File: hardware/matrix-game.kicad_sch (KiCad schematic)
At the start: 31 parts, among them SW1 button_center, SW2 button_left, SW3 button_down, SW4 button_right, SW5 button_up, U1 NUCLEO-F042K6, U2 MAX7219, U3 DM-OLED096-636

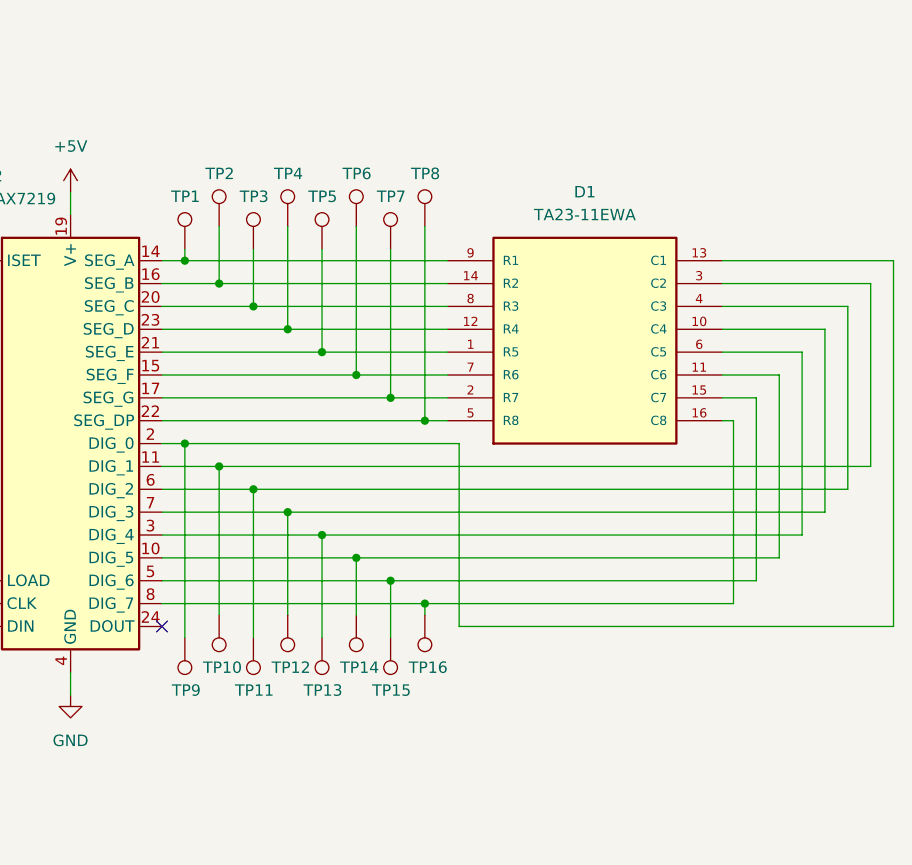
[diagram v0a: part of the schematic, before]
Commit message: [hardware] Replaced old TP pins with a 1x16, 2.54mm pin header
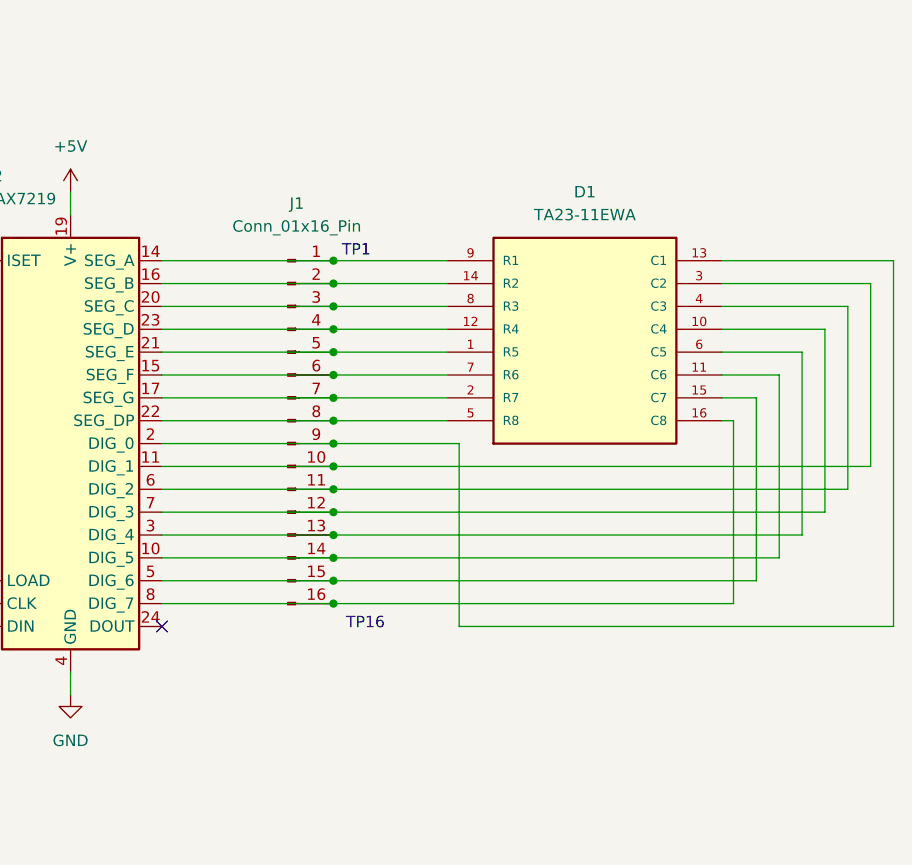
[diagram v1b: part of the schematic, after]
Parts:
- removed TP1, TP10, TP11, TP12, TP13, TP14, TP15, TP16, TP2, TP3, TP4, TP5, TP6, TP7, TP8, TP9: TestPoint, Connector_PinHeader_2.54mm:PinHeader_1x01_P2.54mm_Vertical, symbol Connector:TestPoint
- added J1: Conn_01x16_Pin, Connector_PinHeader_2.54mm:PinHeader_1x16_P2.54mm_Vertical, symbol Connector:Conn_01x16_Pin
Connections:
- net at D1.14 (R2), U2.16 (SEG_B): now also J1.2 (Pin_2)
- net at D1.9 (R1), U2.14 (SEG_A): now also J1.1 (Pin_1)
- net at D1.7 (R6), U2.15 (SEG_F): now also J1.6 (Pin_6)
- net at D1.4 (C3), U2.6 (DIG_2): now also J1.11 (Pin_11)
- net at D1.8 (R3), U2.20 (SEG_C): now also J1.3 (Pin_3)
- net at D1.11 (C6), U2.10 (DIG_5): now also J1.14 (Pin_14)
- net at D1.3 (C2), U2.11 (DIG_1): now also J1.10 (Pin_10)
- net at D1.2 (R7), U2.17 (SEG_G): now also J1.7 (Pin_7)
- net at D1.13 (C1), U2.2 (DIG_0): now also J1.9 (Pin_9)
- net at D1.1 (R5), U2.21 (SEG_E): now also J1.5 (Pin_5)
- net at D1.5 (R8), U2.22 (SEG_DP): now also J1.8 (Pin_8)
- net at D1.12 (R4), U2.23 (SEG_D): now also J1.4 (Pin_4)
- net at D1.6 (C5), U2.3 (DIG_4): now also J1.13 (Pin_13)
- net at D1.15 (C7), U2.5 (DIG_6): now also J1.15 (Pin_15)
- net at D1.10 (C4), U2.7 (DIG_3): now also J1.12 (Pin_12)
- net at D1.16 (C8), U2.8 (DIG_7): now also J1.16 (Pin_16)
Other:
- note added: "TP1"
- note added: "TP16"
